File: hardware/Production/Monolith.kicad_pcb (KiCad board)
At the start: 6 copper layers, 43.2 x 74.4 mm, 307 parts, among them J105 Cell 2 NTC wires, J106 Cell 3 NTC wires, J108 PACK- power wire, J109 CELL1 sense wire, J110 CELL2 sense wire, J111 CELL3 sense wire, J112 PACK+ power wire, J113 LOAD PACK_P, J114 LOAD GND, J115 1N Kelvin wire, J116 4P Kelvin wire, J301 TC2030-NL, J302 TC2030-NL GAUGE, J401 TYPE-C 16PCB1.6 IP68, J501 TYPE-C 16PCB1.6 IP68, Q101 BSC007N04LS6, Q102 BSC007N04LS6, Q103 AO3400A, Q104 AO3400A, Q401 SiZ240DT, Q402 SiZ240DT, Q409 AO3400A, Q501 SiZ240DT, Q502 SiZ240DT, Q509 AO3400A, U101 BQ40Z50RSMR-R2, U102 BQ294700DSGR, U204 TPS62177DQCR, U301 CC2340R5MODA, U401 TPS25751DREFR, U402 M24512-DFMC6TG, U403 BQ25756RRVR, U404 TPS62933DRLR, U405 TPD6S300RUKR, U406 TPS7A4101DGNR, U501 TPS25751DREFR, U502 M24512-DFMC6TG, U503 BQ25756RRVR, U504 TPS62933DRLR, U505 TPD6S300RUKR, U506 TPS7A4101DGNR

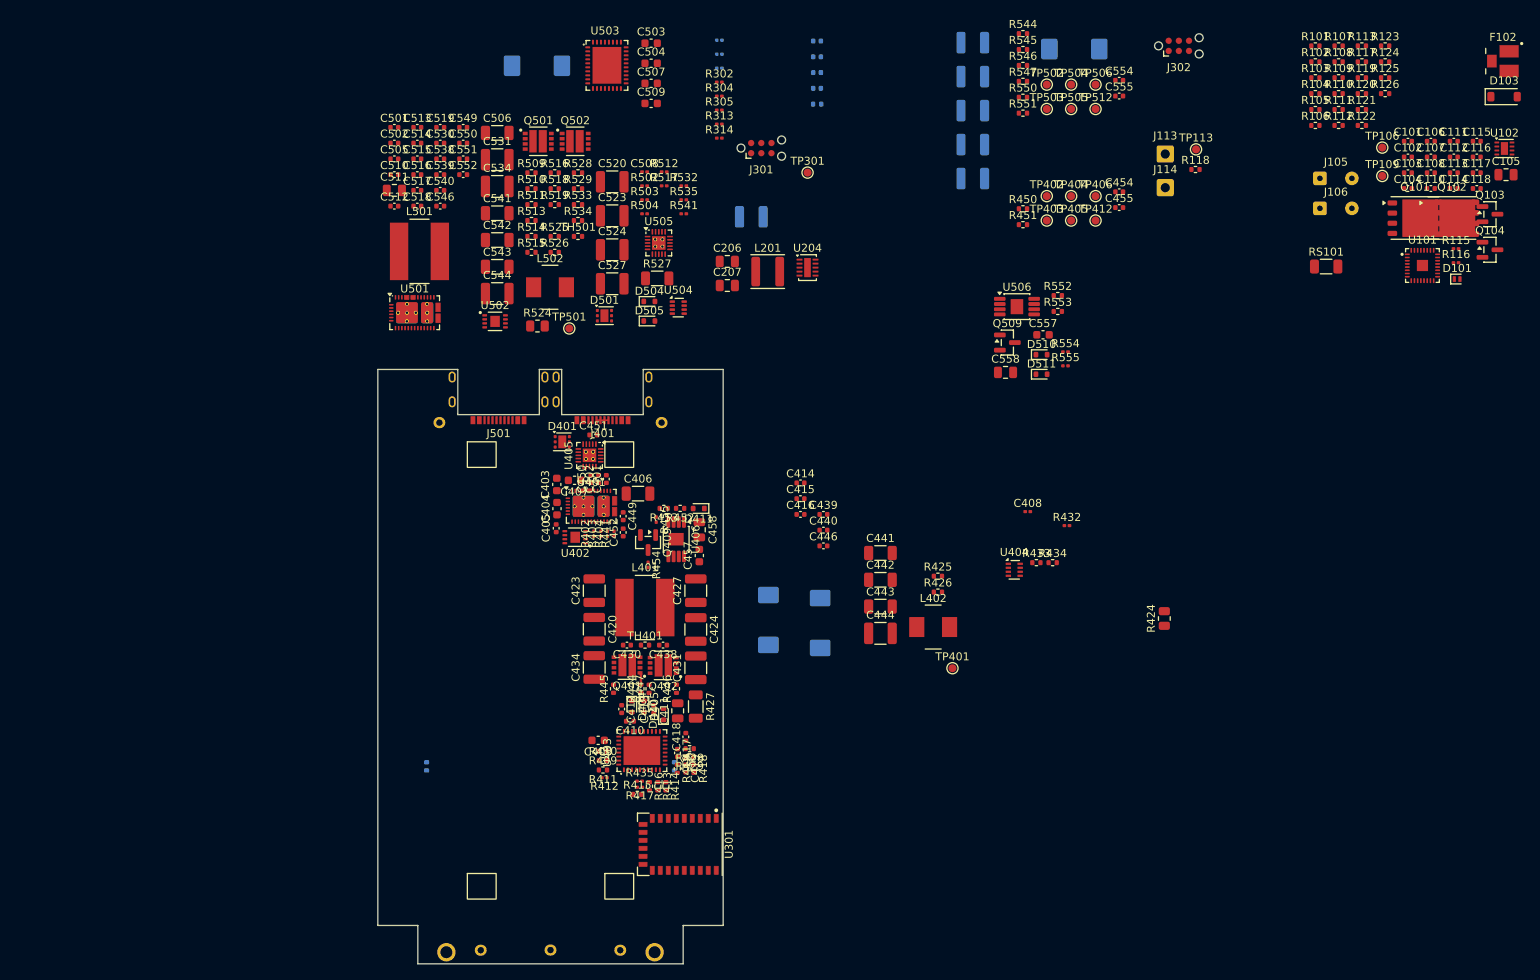
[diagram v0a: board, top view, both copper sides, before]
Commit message: Most of USB Power stages placement done
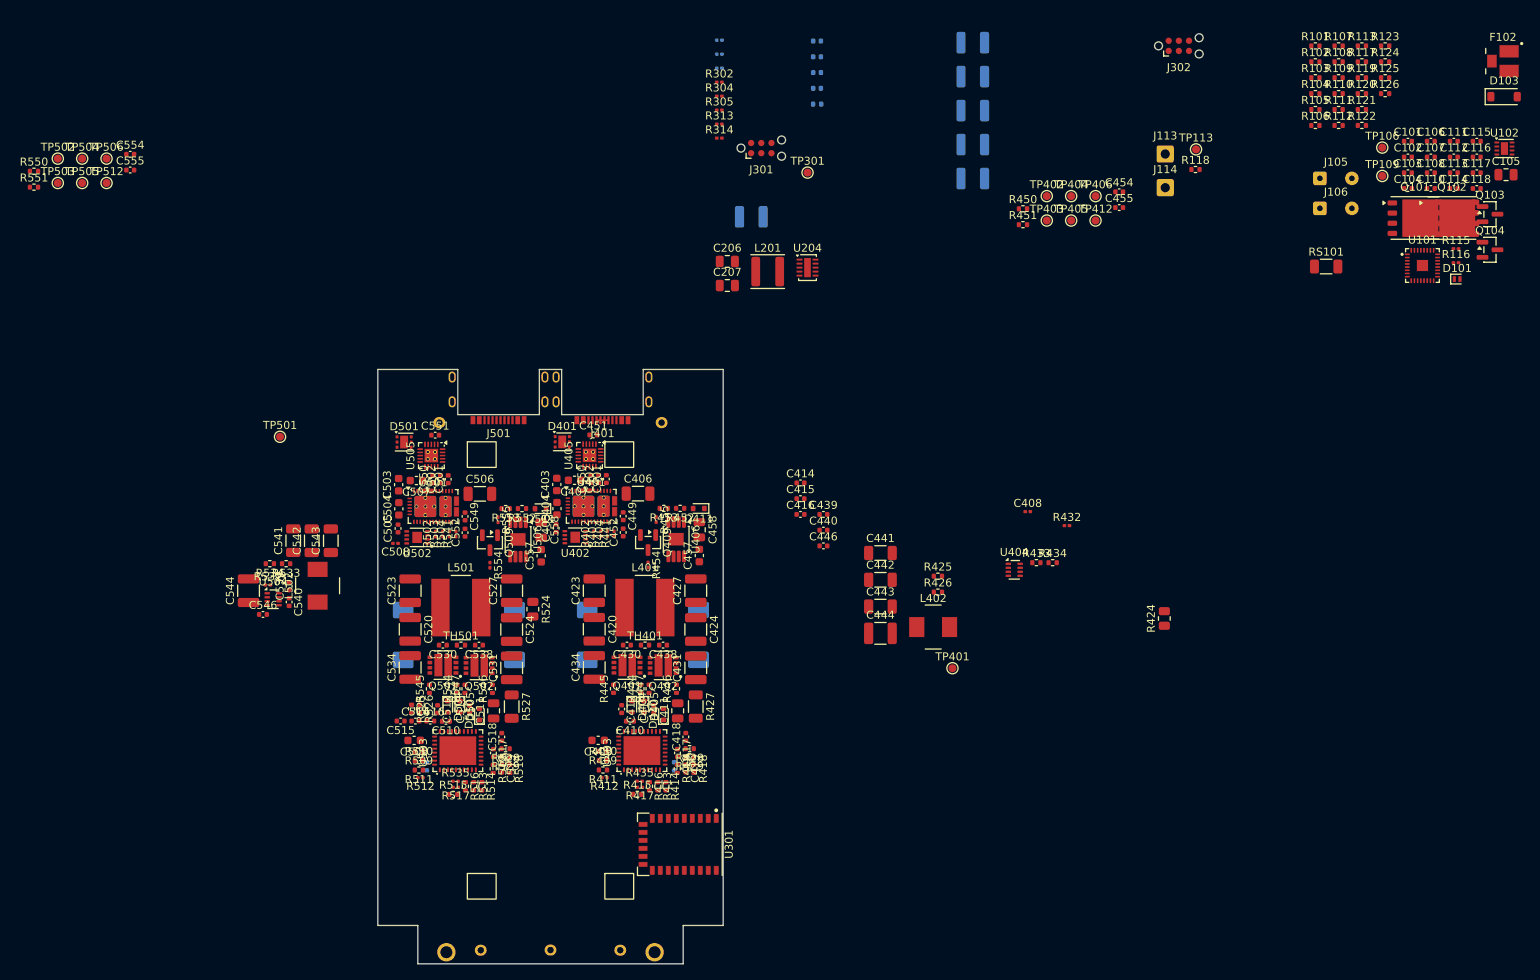
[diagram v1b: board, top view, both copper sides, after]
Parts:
- moved TP502 124.1 mm to (38.4, 36.5)
- moved TP503 124.1 mm to (38.4, 39.5)
- moved TP506 124.1 mm to (44.5, 36.5)
- moved TP512 124.1 mm to (44.5, 39.5)
- moved R550 124.1 mm to (35.4, 38.0)
- moved R551 124.1 mm to (35.4, 40.0)
- moved TP504 124.1 mm to (41.4, 36.5)
- moved TP505 124.1 mm to (41.4, 39.5)
- moved C554 124.1 mm to (47.4, 35.9)
- moved C555 124.1 mm to (47.4, 37.9)
- moved C556 111.5 mm to (81.6, 96.0), turned to -90 degrees
- moved R545 109.1 mm to (84.9, 102.8), turned to 90 degrees
- moved R544 108.3 mm to (88.3, 102.8), turned to 90 degrees
- moved R547 103.2 mm to (89.3, 102.8), turned to 90 degrees
- moved R546 102.4 mm to (92.7, 102.8), turned to 90 degrees
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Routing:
- net /USB Port 1/HG1: track 1.52 -> 0.00 mm

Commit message: Buck done
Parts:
- moved R432 69.9 mm to (101.2, 111.8), turned to 90 degrees
- moved R434 67.6 mm to (99.8, 111.5), turned to -90 degrees
- moved R433 65.0 mm to (99.8, 109.4), turned to -90 degrees
- moved U404 59.8 mm to (102.9, 111.1), turned to 90 degrees
- moved C441 50.0 mm to (96.8, 108.6), turned to 180 degrees
- moved C442 47.6 mm to (96.8, 106.2), turned to 180 degrees
- moved L402 46.6 mm to (102.5, 105.5), turned to 180 degrees
- moved C443 45.9 mm to (96.8, 103.9), turned to 180 degrees
- moved C543 44.2 mm to (64.1, 127.6), turned to 0 degrees
- moved C444 43.5 mm to (101.8, 114.2), turned to 180 degrees
- moved C439 43.2 mm to (101.3, 109.1), turned to 180 degrees
- moved C542 41.5 mm to (64.1, 125.3), turned to 0 degrees
- moved C440 40.5 mm to (103.2, 109.1)
- moved C446 40.2 mm to (104.8, 112.4), turned to 90 degrees
- moved C541 38.9 mm to (64.1, 122.9), turned to 0 degrees
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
